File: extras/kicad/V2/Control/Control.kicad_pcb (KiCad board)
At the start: 2 copper layers, 181.3 x 110 mm, 52 parts, among them J1 Ultrasonic Ranging, J2 Conn_01x05, J3 Output, J4 Input, J6 left, J7 right, P8 BeagleBone_Black_Header, P9 BeagleBone_Black_Header, U1 SparkFun-micromod, U2 ESP-01-WIFI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

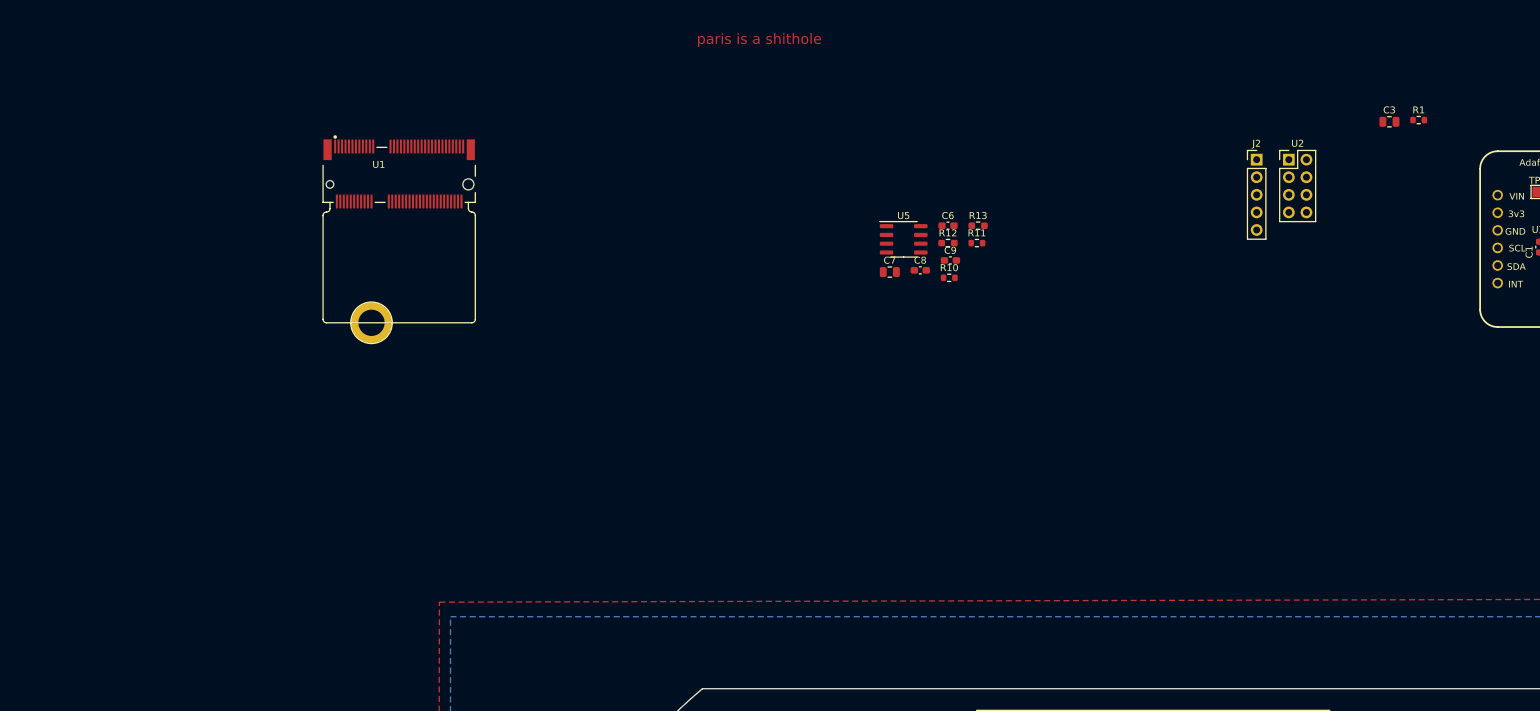
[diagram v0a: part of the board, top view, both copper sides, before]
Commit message: Added larger M.2 & Mikro click board footprints
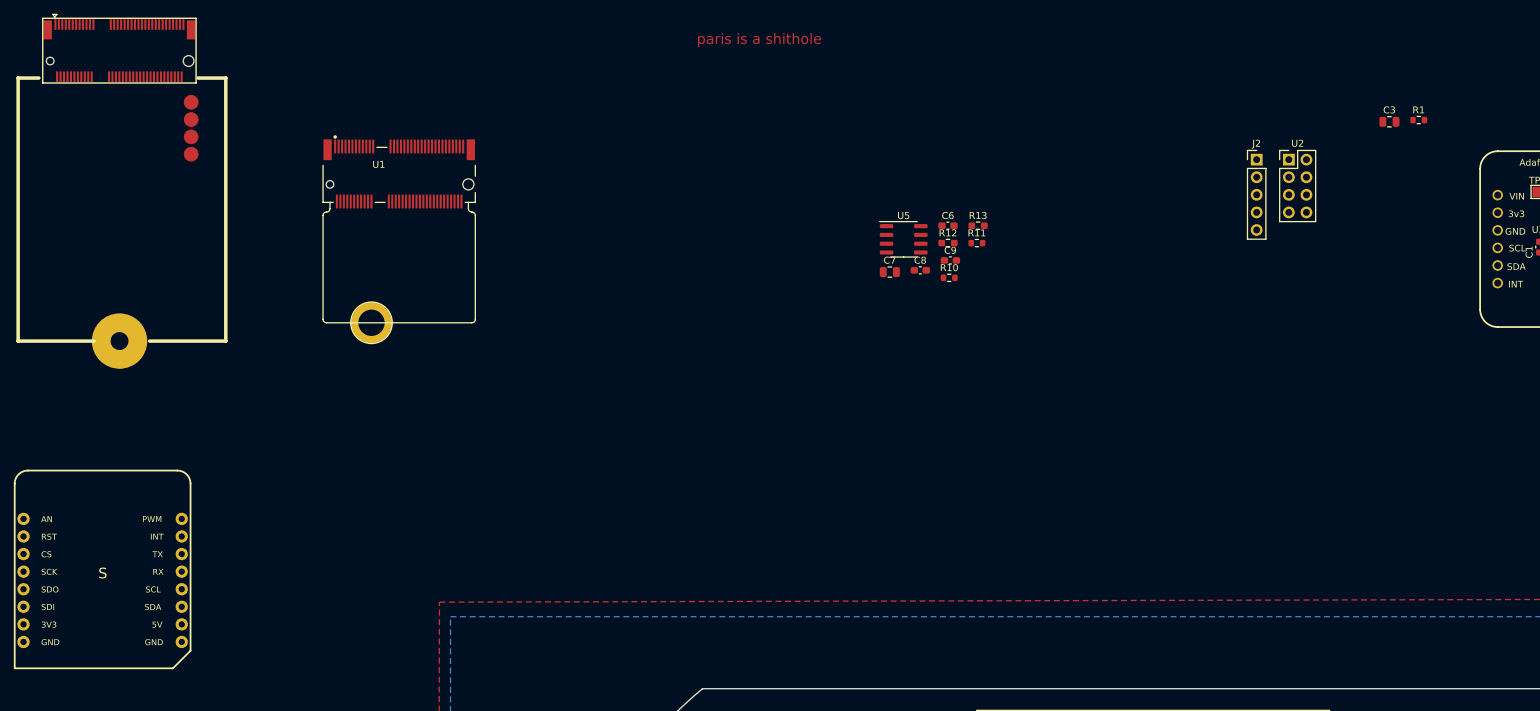
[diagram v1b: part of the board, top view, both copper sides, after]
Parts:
- added ?: , clipboard:4a2d46bf-e065-41e2-839f-8a15f604c178, F.Cu at (-5.08, -7.62)
- added ?: , clipboard:7f5c98d7-2b7a-4a70-a055-24f971a86834, F.Cu at (-10.2, 35.6)

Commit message: k
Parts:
- removed ?: , clipboard:4a2d46bf-e065-41e2-839f-8a15f604c178
- removed ?: , clipboard:7f5c98d7-2b7a-4a70-a055-24f971a86834
- removed C6: 100n, Capacitor_SMD:C_0603_1608Metric_Pad1.08x0.95mm_HandSolder
- removed U2: ESP-01-WIFI, Connector_PinHeader_2.54mm:PinHeader_2x04_P2.54mm_Vertical
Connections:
- J2 pad 2: INT -> /INT_1
- P9 pad 19: /I2C2.SCL -> SCL
- P9 pad 20: /I2C2.SDA -> SDA
- P9 pad 29: /SPI1.D0 -> SPI_MISO
- P9 pad 30: /GPIO[122] -> SPI_MOSI
- P9 pad 31: /SPI1.SCLK -> SPI_SCK
- U1 pad 10: unconnected-(U1-Pad10) -> PWMA_1
- U1 pad 16: INT -> /INT_1
- U1 pad 17: unconnected-(U1-Pad17) -> /Green_4
- U1 pad 18: unconnected-(U1-Pad18) -> PWMA_2
- U1 pad 19: unconnected-(U1-Pad19) -> /yellow_4
- U1 pad 32: unconnected-(U1-Pad32) -> PWMB_1
- U1 pad 33: unconnected-(U1-Pad33) -> GND
- U1 pad 34: unconnected-(U1-Pad34) -> BIN1_1
- U1 pad 38: unconnected-(U1-Pad38) -> BIN2_1
- U1 pad 40: /INT_1 -> AIN1_1
- U1 pad 41: /CAN_RX -> unconnected-(U1-Pad41)
- U1 pad 42: /INT_2 -> AIN2_1
- U1 pad 43: /CAN_TX -> unconnected-(U1-Pad43)
- U1 pad 44: /Ultra_sound_Trig -> AIN2_2
- U1 pad 46: /Ultra_sound_Sig -> BIN1_2
- U1 pad 47: /CAN_STB -> PWMB_2
- U1 pad 48: AIN1_1 -> AIN1_2
- U1 pad 49: BIN2_1 -> unconnected-(U1-Pad49)
- U1 pad 50: AIN2_1 -> /yellow_3
- U1 pad 51: BIN1_1 -> /Green_2
- U1 pad 52: PWMA_1 -> /Green_3
- U1 pad 53: PWMA_2 -> /yellow_2
- U1 pad 54: AIN2_2 -> /yellow_1
- U1 pad 55: BIN2_2 -> SCL
- U1 pad 56: BIN1_2 -> /Green_1
- U1 pad 57: PWMB_2 -> SPI_SCK
- U1 pad 58: PWMB_1 -> unconnected-(U1-Pad58)
- U1 pad 59: +3V3 -> SPI_MISO
- U1 pad 6: unconnected-(U1-Pad6) -> RESET
- U1 pad 60: AIN1_2 -> unconnected-(U1-Pad60)
- U1 pad 61: +3V3 -> SPI_MOSI
- U1 pad 63: +3V3 -> unconnected-(U1-Pad63)
- U1 pad 65: +3V3 -> unconnected-(U1-Pad65)
- U1 pad 67: +3V3 -> unconnected-(U1-Pad67)
- U1 pad 69: +3V3 -> unconnected-(U1-Pad69)
- U1 pad 71: +3V3 -> unconnected-(U1-Pad71)
- U1 pad 73: +3V3 -> BIN2_2
- U4 pad 6: unconnected-(U4-Pad6) -> /INT_1
- U6 pad 10: /Green_2 -> unconnected-(U6-Pad10)
- U6 pad 11: /yellow_3 -> unconnected-(U6-Pad11)
- U6 pad 12: /Green_3 -> unconnected-(U6-Pad12)
- U6 pad 13: /yellow_4 -> unconnected-(U6-Pad13)
- U6 pad 14: /Green_4 -> unconnected-(U6-Pad14)
- U6 pad 6: /yellow_1 -> unconnected-(U6-Pad6)
- U6 pad 7: /Green_1 -> unconnected-(U6-Pad7)
- U6 pad 9: /yellow_2 -> unconnected-(U6-Pad9)

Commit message: f
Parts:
- removed C3: 22u, Capacitor_SMD:C_0805_2012Metric
- removed R1: 10k, Resistor_SMD:R_0603_1608Metric
- removed TP1, TP2, TP3: TestPoint, TestPoint:TestPoint_Pad_1.5x1.5mm
- removed U3: LIS3DHTR, digikey-footprints:VFLGA-16_3x3mm
- added U2: MPU-6050, Sensor_Motion:InvenSense_QFN-24_4x4mm_P0.5mm, F.Cu at (187.0, -26.6)
- moved JP1 7.36 mm to (192.5, -27.5), turned to -90 degrees
- moved C1 5.33 mm to (187.0, -30.1), turned to 180 degrees
- moved C2 2.44 mm to (190.4, -26.6), turned to 90 degrees
- moved JP2 0.67 mm to (192.4, -22.7)
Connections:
- J1 pad 2: /Ultra_sound_Sig -> SDA
- J1 pad 3: /Ultra_sound_Trig -> SCL

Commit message: f
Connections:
- J6 pad 21: +3V3 -> GND
- J6 pad 33: +3V3 -> GND
- J7 pad 32: +3V3 -> GND
- J7 pad 40: +3V3 -> GND
- P9 pad 17: /GPIO[4] -> SPI_CS
- U1 pad 55: SCL -> SPI_CS
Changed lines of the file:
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@@
   (net 169 "/GPIO[48]")
   (net 170 "/GPIO[51]")
-  (net 171 "/GPIO[4]")
+  (net 171 "SPI_CS")
   (net 172 "/GPIO[5]")
   (net 173 "unconnected-(U6-Pad10)")
@@
       (net 17 "/yellow_1") (pinfunction "AUD_IN") (pintype "input"))
     (pad "55" smd rect (at 4.25 -3.97) (size 0.3 2) (layers "F.Cu" "F.Paste" "F.Mask")
-      (net 2 "SCL") (pinfunction "SPI_CS") (pintype "input"))
+      (net 171 "SPI_CS") (pinfunction "SPI_CS") (pintype "input"))
     (pad "56" smd rect (at 4.5 3.98) (size 0.3 2) (layers "F.Cu" "F.Paste" "F.Mask")
       (net 19 "/Green_1") (pinfunction "AUD_OUT") (pintype "input"))
@@
       (net 1 "GND") (pinfunction "Pin_20") (pintype "passive"))
     (pad "21" thru_hole oval (at 0 25.4 90) (size 1.7 1.7) (drill 1) (layers F&B.Cu *.Mask)
-      (net 4 "+3V3") (pinfunction "Pin_21") (pintype "passive"))
+      (net 1 "GND") (pinfunction "Pin_21") (pintype "passive"))
     (pad "22" thru_hole oval (at 2.54 25.4 90) (size 1.7 1.7) (drill 1) (layers F&B.Cu *.Mask)
       (net 14 "unconnected-(J6-Pad22)") (pinfunction "Pin_22") (pintype "passive"))
@@
       (net 1 "GND") (pinfunction "Pin_32") (pintype "passive"))
     (pad "33" thru_hole oval (at 0 40.64 90) (size 1.7 1.7) (drill 1) (layers F&B.Cu *.Mask)
-      (net 4 "+3V3") (pinfunction "Pin_33") (pintype "passive"))
+      (net 1 "GND") (pinfunction "Pin_33") (pintype "passive"))
     (pad "34" thru_hole oval (at 2.54 40.64 90) (size 1.7 1.7) (drill 1) (layers F&B.Cu *.Mask)
       (net 23 "BIN1_1") (pinfunction "Pin_34") (pintype "passive"))
@@
       (net 1 "GND") (pinfunction "Pin_31") (pintype "passive"))
     (pad "32" thru_hole oval (at 2.54 38.1 90) (size 1.7 1.7) (drill 1) (layers F&B.Cu *.Mask)
-      (net 4 "+3V3") (pinfunction "Pin_32") (pintype "passive"))
+      (net 1 "GND") (pinfunction "Pin_32") (pintype "passive"))
     (pad "33" thru_hole oval (at 0 40.64 90) (size 1.7 1.7) (drill 1) (layers F&B.Cu *.Mask)
       (net 50 "unconnected-(J7-Pad33)") (pinfunction "Pin_33") (pintype "passive"))
@@
       (net 55 "unconnected-(J7-Pad39)") (pinfunction "Pin_39") (pintype "passive"))
     (pad "40" thru_hole oval (at 2.54 48.26 90) (size 1.7 1.7) (drill 1) (layers F&B.Cu *.Mask)
-      (net 4 "+3V3") (pinfunction "Pin_40") (pintype "passive"))
+      (net 1 "GND") (pinfunction "Pin_40") (pintype "passive"))
     (model "${KICAD6_3DMODEL_DIR}/Connector_PinHeader_2.54mm.3dshapes/PinHeader_2x20_P2.54mm_Vertical.wrl"
       (offset (xyz 0 0 0))
@@
     (descr "24-Lead Plastic QFN (4mm x 4mm); Pitch 0.5mm; EP 2.7x2.6mm; for InvenSense motion sensors; keepout area marked (Package see: https://store.invensense.com/datasheets/invensense/MPU-6050_DataSheet_V3%204.pdf; See also https://www.invensense.com/wp-content/uploads/2015/02/InvenSense-MEMS-Handling.pdf)")
     (tags "QFN 0.5")
+    (property "LCSC" "C50278")
     (property "Sheetfile" "Control.kicad_sch")
     (property "Sheetname" "")
@@
     (fp_arc (start 10.883614 -12.0415) (mid 12.657311 -11.285145) (end 13.388855 -9.501066) (layer "F.SilkS") (width 0.254))
     (fp_arc (start -12.011386 -9.5015) (mid -11.267437 -11.297551) (end -9.471386 -12.0415) (layer "F.SilkS") (width 0.254))
-    (fp_arc (start 13.389614 8.2945) (mid 12.651813 10.068874) (end 10.882752 10.819321) (layer "F.SilkS") (width 0.254))
+    (fp_arc (start 13.389614 8.2945) (mid 12.651812 10.06887) (end 10.882752 10.819321) (layer "F.SilkS") (width 0.254))
     (fp_arc (start -9.505386 10.8185) (mid -11.279706 10.062522) (end -12.011614 8.278139) (layer "F.SilkS") (width 0.254))
     (fp_line (start 13.388614 10.8185) (end -12.011386 10.8185) (layer "F.CrtYd") (width 0.152))
@@
       (net 170 "/GPIO[51]") (pinfunction "Pin_16") (pintype "passive"))
     (pad "17" thru_hole oval locked (at 0 -20.32 270) (size 1.7 1.7) (drill 1) (layers F&B.Cu *.Mask)
-      (net 171 "/GPIO[4]") (pinfunction "Pin_17") (pintype "passive"))
+      (net 171 "SPI_CS") (pinfunction "Pin_17") (pintype "passive"))
     (pad "18" thru_hole oval locked (at 2.54 -20.32 270) (size 1.7 1.7) (drill 1) (layers F&B.Cu *.Mask)
       (net 172 "/GPIO[5]") (pinfunction "Pin_18") (pintype "passive"))
